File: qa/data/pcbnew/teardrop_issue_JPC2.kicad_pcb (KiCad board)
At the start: 2 copper layers, 1 part

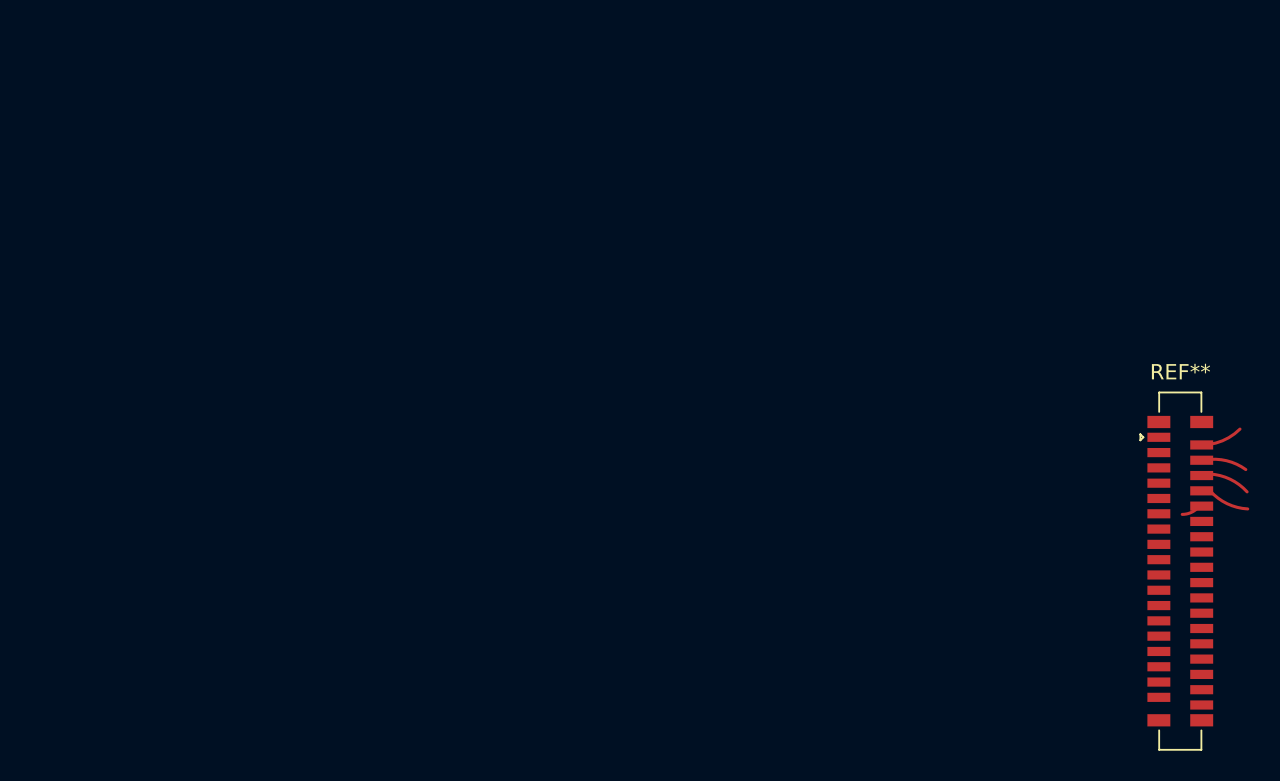
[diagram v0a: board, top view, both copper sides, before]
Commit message: feat: update kicad to 9.0.0+dfsg-1
Signed-off-by: lhdjply <lhdjply@126.com>
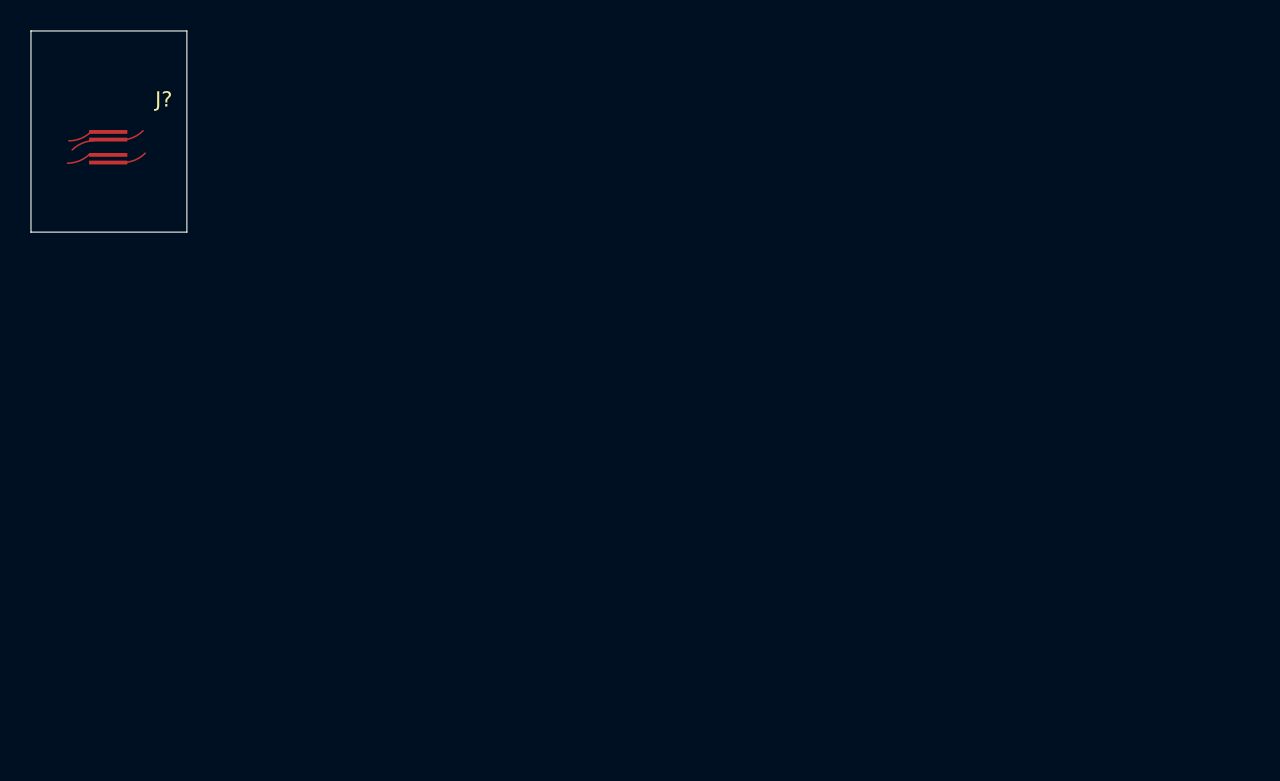
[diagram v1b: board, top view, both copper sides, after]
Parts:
- removed REF**: Molex_52559-3652_2x18-1MP_P0.5mm_Vertical, Connector_FFC-FPC:Molex_52559-3652_2x18-1MP_P0.5mm_Vertical
- added J?: Vision_Module, Don-Con:FFC_Pads_01x22_P0.5mm_3mm-stiffener, F.Cu at (66.4, 53.8)
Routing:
- net /SYNC_ZRGB: track 0.00 -> 3.26 mm
- net GND: track 0.00 -> 3.26 mm
- net C: track 2.76 -> 0.00 mm
- net e: track 2.76 -> 0.00 mm
- net B: track 2.76 -> 0.00 mm
- net A: track 2.76 -> 0.00 mm
- net /OUT_CAM0_SCL: track 0.00 -> 1.63 mm
- net f: track 1.10 -> 0.00 mm
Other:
- board outline added: 10.2 x 13.1 mm
